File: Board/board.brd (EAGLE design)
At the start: 131 x 95.4 mm, 49 parts, among them IC1 L297, IC2 MEGA32-P, IC3 L298, J1 +12V, Q1 BC639, Q3 BC639, U1 MCP9808MSOP, X1 WATER_PUMP, X2 FAN, X5 SM_CD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

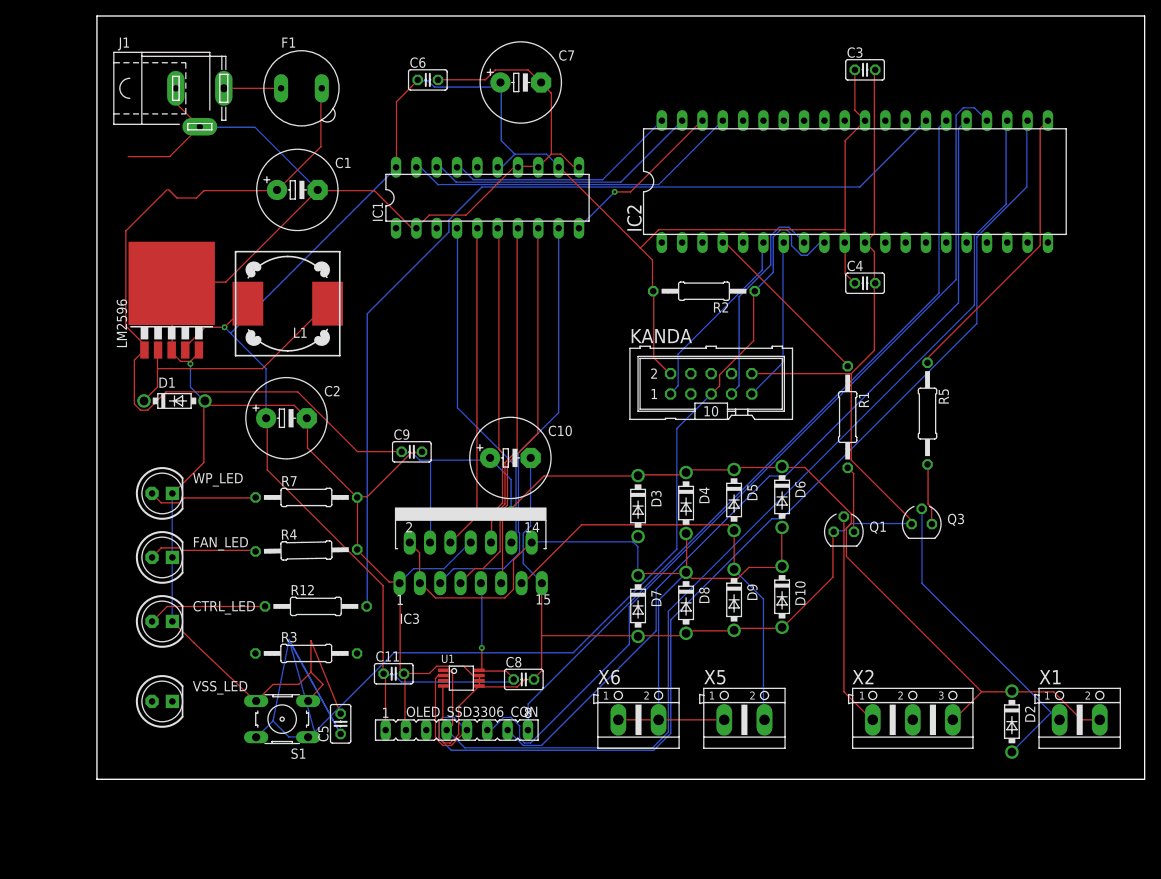
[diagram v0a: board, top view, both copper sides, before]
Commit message: added 5mm vss led
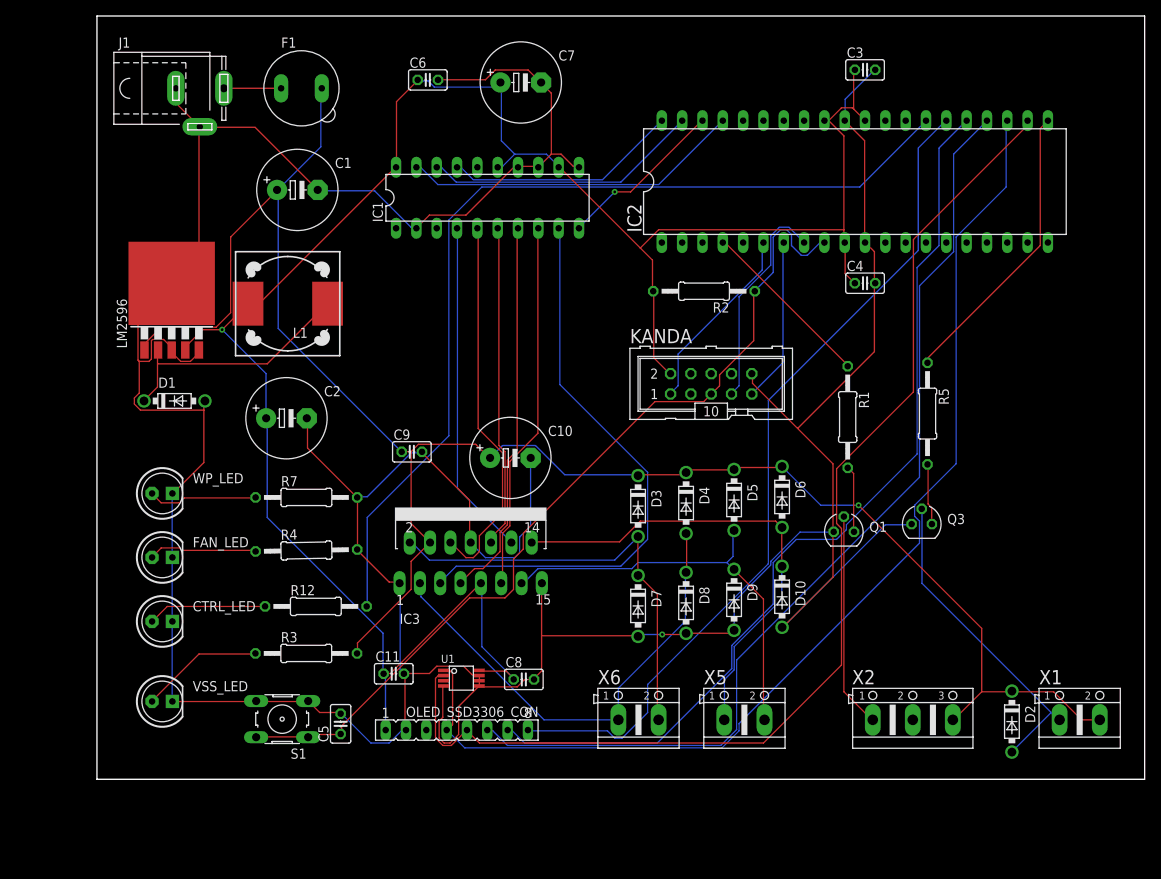
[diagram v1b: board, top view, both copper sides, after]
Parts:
- R1, R5: value (none) -> 220R
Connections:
- removed net AGND: IC2.31
- removed net AREF: IC2.32
- removed net VSS1: D10.C, D3.A, D4.A, D6.A, D7.C, D8.C, IC3.14, IC3.2, IC3.3, X5.1, X6.1, X6.2
- new net N$24: D10.C, D6.A, IC3.14, X5.1
- new net N$25: D3.A, D7.C, IC3.2, X6.2
- net GND: now also IC2.31
- net N$26: now also D4.A, D8.C, IC3.3, X6.1; no longer IC2.3
- net VCC: now also IC2.32
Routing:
- net VSS1: track 105.5 -> 0.00 mm
- net N$24: track 0.00 -> 59.9 mm
- net N$26: track 0.00 -> 59.7 mm
- net N$25: track 0.00 -> 54.8 mm
- net N$10: track 165.6 -> 111.0 mm
- net GND: track 486.9 -> 511.9 mm
- net N$13: track 54.3 -> 71.8 mm
- net N$7: track 0.00 -> 15.4 mm
- net N$38: track 106.3 -> 116.1 mm
- net N$39: track 97.9 -> 106.2 mm
- net N$37: track 113.7 -> 121.9 mm
- net N$15: track 40.7 -> 47.7 mm
- net N$35: track 132.1 -> 137.7 mm
- net VSS: track 225.3 -> 229.2 mm
- net VCC: track 260.9 -> 264.1 mm, vias 2 -> 1
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
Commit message: gnd line
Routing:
- net GND: track 511.9 -> 44.9 mm, vias 1 -> 0
- net N$37: track 121.9 -> 170.9 mm
- net VSS: track 229.2 -> 260.6 mm, vias 1 -> 0
- net N$35: track 137.7 -> 119.6 mm, vias 0 -> 1
- net N$13: track 71.8 -> 56.5 mm, vias 0 -> 1
- net N$38: track 116.1 -> 101.2 mm, vias 0 -> 1
- net N$27: track 52.9 -> 67.7 mm
- net N$25: track 54.8 -> 68.3 mm
- net N$2: track 31.5 -> 42.4 mm
- net N$26: track 59.7 -> 70.4 mm
- net N$56: track 48.0 -> 58.6 mm, vias 0 -> 1
- net N$6: track 20.6 -> 31.1 mm
- net N$5: track 22.1 -> 32.4 mm
- net N$39: track 106.2 -> 97.9 mm, vias 0 -> 1
- net N$10: track 111.0 -> 104.6 mm
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- added copper zone on layer 16, net GND
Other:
- board size 131 x 95.4 mm -> 129 x 93.4 mm

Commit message: ds
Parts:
- removed U1: MCP9808MSOP, MCP9808:MSOP-8
- added R6, R8: 4K7, rcl:0207/12
- added U2: DS1621+, ds1621p:21-0043D_8
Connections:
- net GND: now also U2.4, U2.5, U2.6, U2.7; no longer U1.4, U1.5, U1.6, U1.7
- net N$35: now also R8.1, U2.2; no longer U1.1
- net N$36: now also R6.1, U2.1; no longer U1.2
- net VCC: now also R6.2, R8.2, U2.8; no longer U1.8
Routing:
- net GND: track 44.9 -> 39.0 mm
- net VCC: track 258.9 -> 258.3 mm

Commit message: rc 1.0
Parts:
- moved U2 135.2 mm to (114.0, -71.0)
- moved R6 124.3 mm to (99.0, -72.0), turned to 90 degrees
- moved R8 122.2 mm to (94.0, -72.0), turned to 90 degrees
- moved C8 83.6 mm to (110.2, -59.2)
- moved OLED_SSD3306_CON 81.0 mm to (110.8, -87.6), turned to 90 degrees
- moved C11 75.0 mm to (98.9, -87.5)
- moved Q3 12.4 mm to (89.9, -101.8)
- moved R5 12.4 mm to (90.7, -88.0)
- moved Q1 11.0 mm to (83.2, -101.8)
- moved R1 11.0 mm to (83.7, -87.5)
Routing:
- net GND: track 39.0 -> 590.4 mm, vias 0 -> 3
- net N$12: track 36.5 -> 129.0 mm, vias 0 -> 4
- net VCC: track 258.3 -> 342.8 mm
- net N$36: track 139.2 -> 67.3 mm, vias 2 -> 1
- net N$37: track 170.9 -> 124.3 mm, vias 0 -> 1
- net N$39: track 97.9 -> 55.6 mm
- net N$10: track 104.6 -> 145.2 mm, vias 0 -> 1
- net N$38: track 101.2 -> 60.8 mm
- net N$13: track 56.5 -> 80.2 mm, vias 1 -> 2
- net N$5: track 32.4 -> 51.6 mm, vias 0 -> 2
- net N$11: track 111.2 -> 129.1 mm, vias 2 -> 1
- net N$35: track 119.4 -> 101.9 mm, vias 1 -> 0
- net N$21: track 52.5 -> 68.9 mm, vias 1 -> 2
- net N$58: track 40.7 -> 54.8 mm, vias 1 -> 2
- net N$56: track 58.6 -> 72.6 mm
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- added copper zone on layer 16, net N$30
- removed copper zone on layer 16, net GND
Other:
- board text added: "SMART HAMSTER CAGE v1 Damian Pozimski @ 2018"

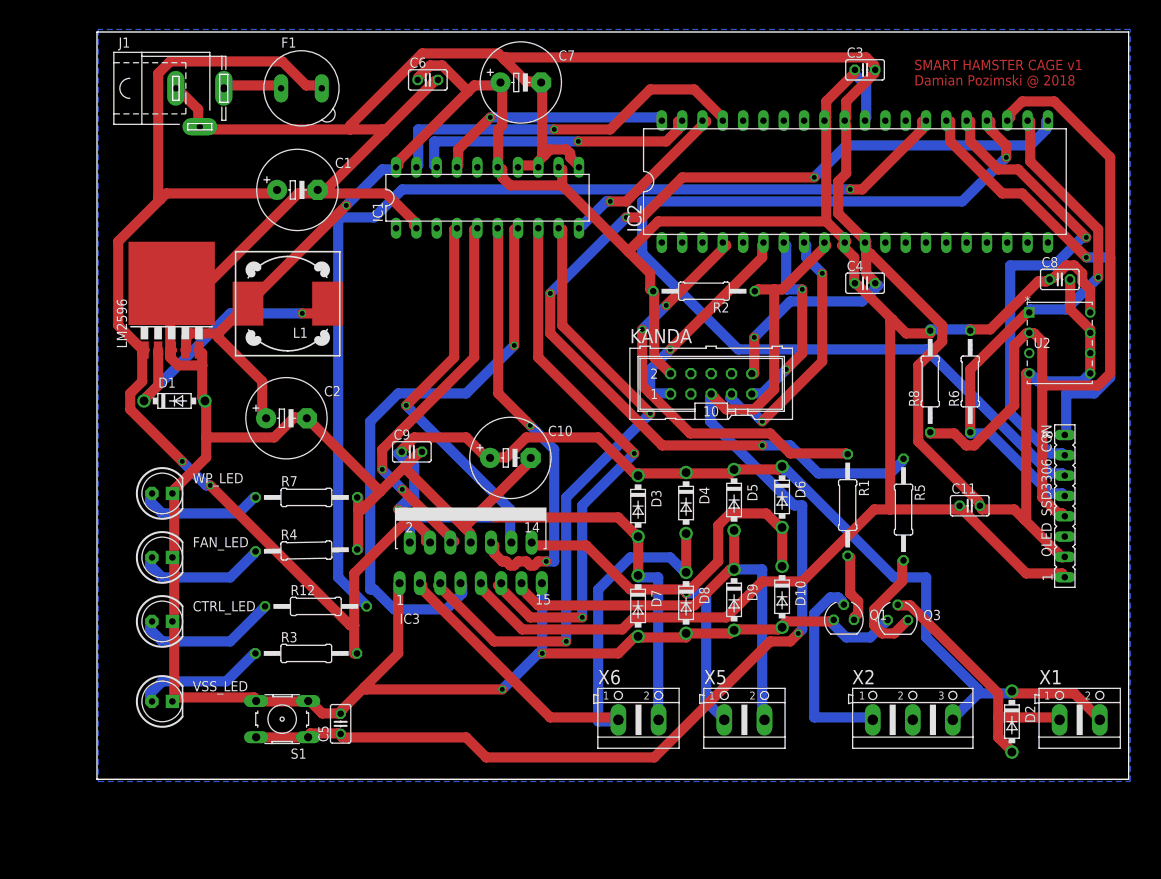
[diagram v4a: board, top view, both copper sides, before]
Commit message: PWM devices code
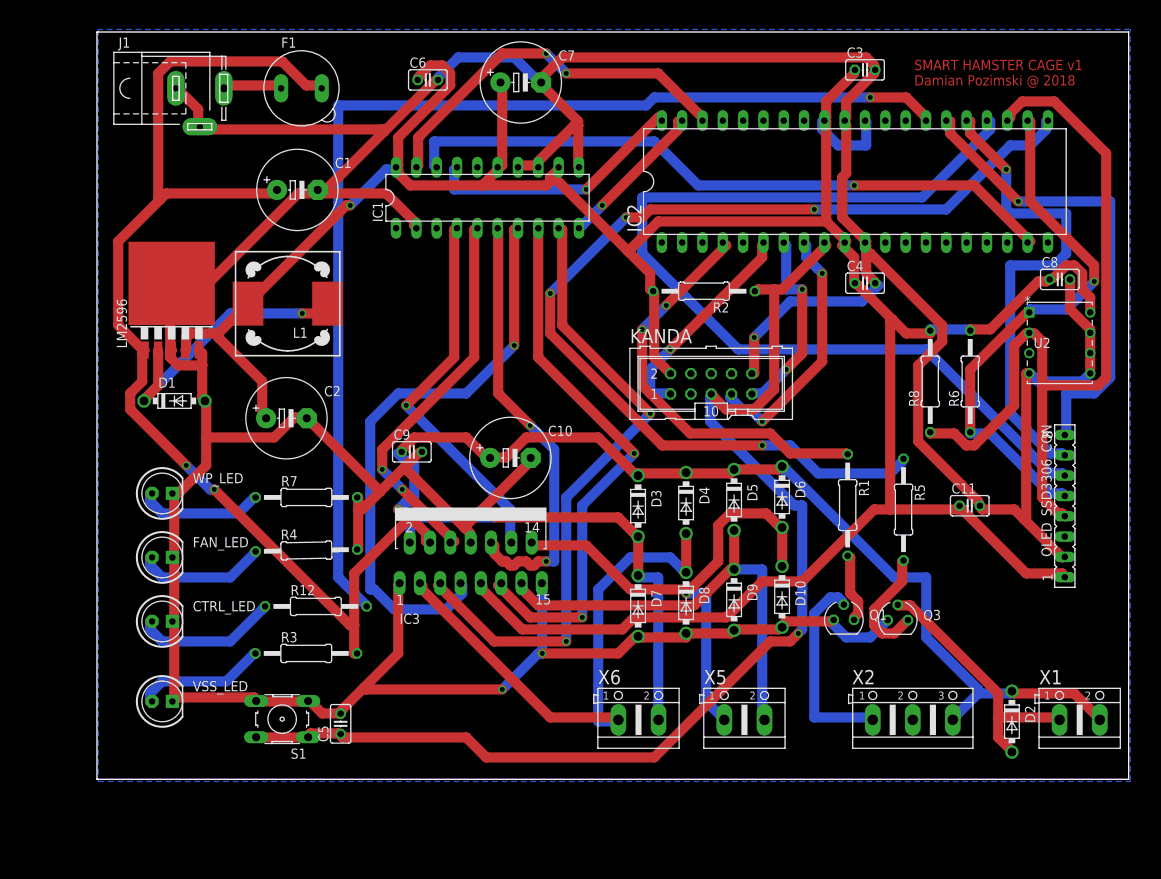
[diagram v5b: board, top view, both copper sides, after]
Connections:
- net N$18: now also IC2.19; no longer IC2.39
- net N$19: now also IC2.39; no longer IC2.38
- net N$20: now also IC2.38; no longer IC2.37
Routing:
- net N$18: track 36.0 -> 83.4 mm
- net GND: track 590.4 -> 576.4 mm
- net VCC: track 342.8 -> 355.8 mm
- net N$11: track 129.1 -> 139.4 mm
- net N$37: track 124.3 -> 119.8 mm, vias 1 -> 0
- net N$39: track 55.6 -> 59.1 mm
- net N$17: track 29.5 -> 32.8 mm
- net N$19: track 21.9 -> 19.0 mm
- net N$20: track 46.8 -> 47.4 mm, vias 1 -> 2

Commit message: Timr0 as counter, Timer1 output b for fan
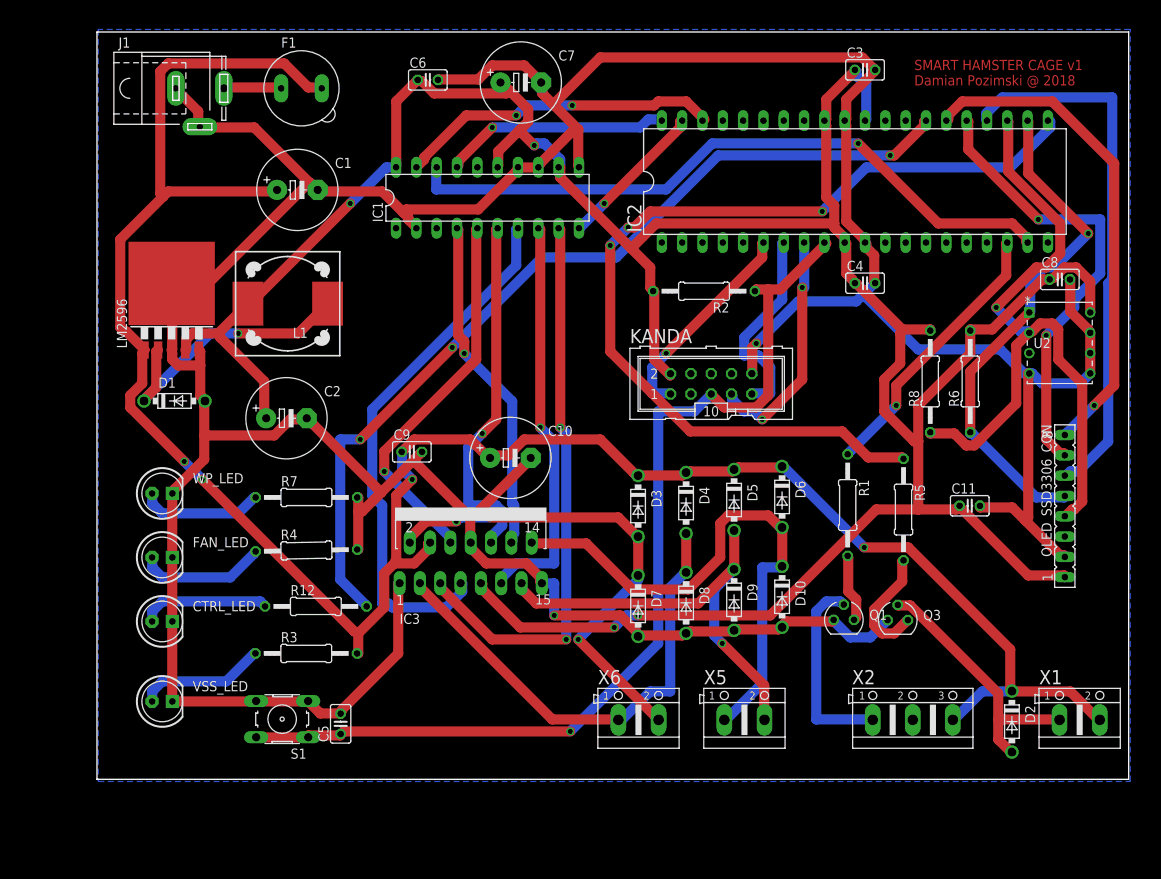
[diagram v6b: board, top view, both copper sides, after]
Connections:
- removed net N$5: IC2.4, R1.1
- new net N$31: IC2.18, R1.1
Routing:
- net N$37: track 119.8 -> 67.9 mm
- net N$5: track 51.6 -> 0.00 mm, vias 2 -> 0
- net GND: track 576.4 -> 524.9 mm, vias 3 -> 2
- net N$31: track 0.00 -> 34.7 mm, vias 0 -> 1
- net N$11: track 139.4 -> 112.2 mm, vias 1 -> 3
- net N$10: track 145.2 -> 125.2 mm
- net N$21: track 68.9 -> 50.8 mm, vias 2 -> 1
- net N$35: track 101.5 -> 88.9 mm, vias 0 -> 1
- net N$12: track 129.0 -> 117.7 mm, vias 4 -> 3
- net N$58: track 54.8 -> 45.3 mm, vias 2 -> 1
- net N$13: track 80.2 -> 70.8 mm
- net N$26: track 69.8 -> 60.7 mm
- net N$20: track 47.4 -> 40.7 mm
- net N$56: track 72.6 -> 67.2 mm, vias 1 -> 0
- net N$16: track 47.4 -> 42.4 mm
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
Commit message: Added new inductor
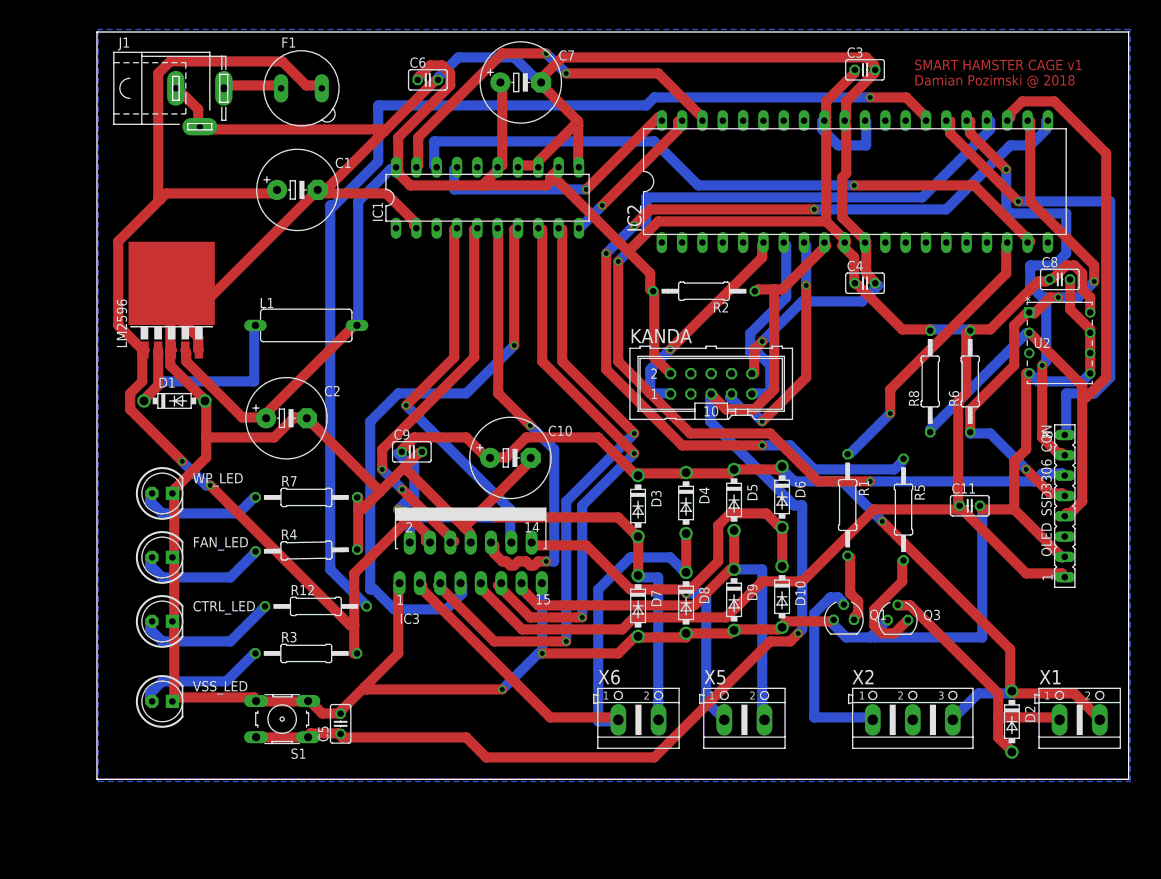
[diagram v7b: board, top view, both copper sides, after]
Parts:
- L1: device inductors:DR127 -> inductors:BC12
- moved L1 3.57 mm to (16.0, -65.0), turned to 0 degrees
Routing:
- net N$37: track 67.9 -> 132.4 mm, vias 0 -> 2
- net GND: track 524.9 -> 569.8 mm, vias 2 -> 3
- net N$11: track 112.2 -> 137.6 mm, vias 3 -> 1
- net N$10: track 125.2 -> 145.2 mm
- net N$21: track 50.8 -> 69.1 mm, vias 1 -> 2
- net N$58: track 45.3 -> 54.8 mm, vias 1 -> 2
- net N$26: track 60.7 -> 69.8 mm
- net N$13: track 70.8 -> 78.5 mm
- net N$20: track 40.7 -> 47.4 mm
- net N$2: track 35.2 -> 29.1 mm, vias 1 -> 0
- net N$56: track 67.2 -> 72.6 mm, vias 0 -> 1
- net N$16: track 42.4 -> 47.4 mm
- net N$17: track 28.4 -> 32.8 mm
- net N$35: track 88.9 -> 93.0 mm, vias 1 -> 0
- net N$24: track 69.2 -> 65.6 mm, vias 0 -> 1
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
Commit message: Resistor value
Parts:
- C1: value 680uF -> 470uF
- D1, D10, D3, D4, D5, D6, D7, D8, D9: value 1N5824 -> 1N5822
- R1, R5: value 220R -> 240R
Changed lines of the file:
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@@
 <attribute name="OC_NEWARK" value="98K6125" x="15.4" y="-35.36" size="1.778" layer="27" display="off"/>
 </element>
-<element name="C1" library="resistor" package="E5-10,5" value="680uF" x="14.89" y="-48.06"/>
-<element name="D1" library="diode" package="DO41-7.6" value="1N5824" x="-0.47" y="-74.44"/>
+<element name="C1" library="resistor" package="E5-10,5" value="470uF" x="14.89" y="-48.06"/>
+<element name="D1" library="diode" package="DO41-7.6" value="1N5822" x="-0.47" y="-74.44"/>
 <element name="C2" library="resistor" package="E5-10,5" value="220uF" x="13.53" y="-76.6"/>
 <element name="IC2" library="avr-7" package="DIL40" value="MEGA32-P" x="84.58" y="-47.02"/>
@@
 <attribute name="OC_NEWARK" value="unknown" x="91.82" y="-114.3" size="1.778" layer="27" display="off"/>
 </element>
-<element name="R1" library="rcl" package="0207/12" value="220R" x="83.68" y="-87.45" rot="R270">
+<element name="R1" library="rcl" package="0207/12" value="240R" x="83.68" y="-87.45" rot="R270">
 <attribute name="SPICEPREFIX" value="R" x="83.68" y="-87.45" size="1.778" layer="27" rot="R270" display="off"/>
 </element>
@@
 </element>
 <element name="D2" library="diode" package="DO41-7.6" value="1N5824" x="104.21" y="-114.52" rot="R270"/>
-<element name="R5" library="rcl" package="0207/12" value="220R" x="90.66" y="-88.02" rot="R270">
+<element name="R5" library="rcl" package="0207/12" value="240R" x="90.66" y="-88.02" rot="R270">
 <attribute name="SPICEPREFIX" value="R" x="107.17" y="-88.02" size="1.778" layer="27" rot="R270" display="off"/>
 </element>
@@
 <attribute name="SPICEPREFIX" value="R" x="16.02" y="-86.5" size="1.778" layer="27" display="off"/>
 </element>
-<element name="D3" library="diode" package="DO41-7.6" value="1N5824" x="57.48" y="-87.58" rot="R270"/>
-<element name="D4" library="diode" package="DO41-7.6" value="1N5824" x="63.48" y="-87.2" rot="R270"/>
-<element name="D5" library="diode" package="DO41-7.6" value="1N5824" x="69.48" y="-86.82" rot="R270"/>
-<element name="D6" library="diode" package="DO41-7.6" value="1N5824" x="75.48" y="-86.44" rot="R270"/>
-<element name="D7" library="diode" package="DO41-7.6" value="1N5824" x="57.48" y="-100.06" rot="R270"/>
-<element name="D8" library="diode" package="DO41-7.6" value="1N5824" x="63.48" y="-99.68" rot="R270"/>
-<element name="D9" library="diode" package="DO41-7.6" value="1N5824" x="69.48" y="-99.3" rot="R270"/>
-<element name="D10" library="diode" package="DO41-7.6" value="1N5824" x="75.48" y="-98.92" rot="R270"/>
+<element name="D3" library="diode" package="DO41-7.6" value="1N5822" x="57.48" y="-87.58" rot="R270"/>
+<element name="D4" library="diode" package="DO41-7.6" value="1N5822" x="63.48" y="-87.2" rot="R270"/>
+<element name="D5" library="diode" package="DO41-7.6" value="1N5822" x="69.48" y="-86.82" rot="R270"/>
+<element name="D6" library="diode" package="DO41-7.6" value="1N5822" x="75.48" y="-86.44" rot="R270"/>
+<element name="D7" library="diode" package="DO41-7.6" value="1N5822" x="57.48" y="-100.06" rot="R270"/>
+<element name="D8" library="diode" package="DO41-7.6" value="1N5822" x="63.48" y="-99.68" rot="R270"/>
+<element name="D9" library="diode" package="DO41-7.6" value="1N5822" x="69.48" y="-99.3" rot="R270"/>
+<element name="D10" library="diode" package="DO41-7.6" value="1N5822" x="75.48" y="-98.92" rot="R270"/>
 <element name="C9" library="rcl" package="C025-025X050" value="100nF" x="29.2" y="-80.8">
 <attribute name="SPICEPREFIX" value="C" x="29.2" y="-1181.89" size="1.778" layer="27" display="off"/>
